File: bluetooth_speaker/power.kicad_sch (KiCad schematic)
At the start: 10 parts, among them U2 XL4015

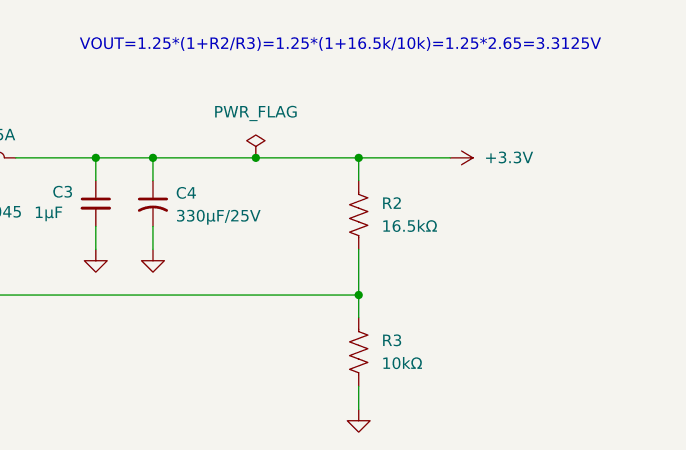
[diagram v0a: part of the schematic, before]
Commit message: adding few footprints
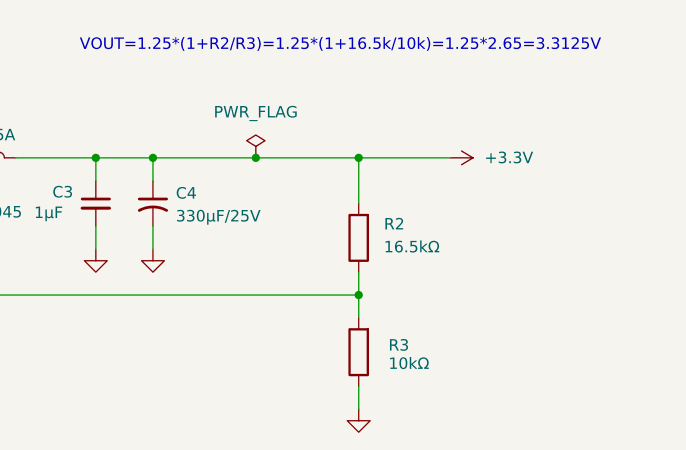
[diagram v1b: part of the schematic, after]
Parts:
- removed R2: 16.5kΩ, symbol Device:R_US
- removed R3: 10kΩ, symbol Device:R_US
- added R2: 16.5kΩ, Resistor_SMD:R_0603_1608Metric_Pad0.98x0.95mm_HandSolder, symbol Device:R
- added R3: 10kΩ, Resistor_SMD:R_0603_1608Metric_Pad0.98x0.95mm_HandSolder, symbol Device:R
- C3, C6, C7: footprint (none) -> Capacitor_SMD:C_0603_1608Metric_Pad1.08x0.95mm_HandSolder
- L1: footprint (none) -> footprints:IND_BOURNS_SDR2207
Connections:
- net +3.3V: now also R2.2
- net GND: now also R3.1
- net at U2.2 (FB): now also R2.1, R3.2
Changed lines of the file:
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@@
 	(wire
 		(pts
-			(xy 167.64 48.26) (xy 167.64 53.34)
+			(xy 167.64 50.8) (xy 167.64 53.34)
 		)
 		(stroke
@@
 	(wire
 		(pts
-			(xy 167.64 40.64) (xy 167.64 38.1)
+			(xy 167.64 43.18) (xy 167.64 38.1)
 		)
 		(stroke
@@
 	)
 	(symbol
-		(lib_id "Device:R_US")
-		(at 167.64 44.45 0)
-		(unit 1)
-		(exclude_from_sim no)
-		(in_bom yes)
-		(on_board yes)
-		(dnp no)
-		(fields_autoplaced yes)
-		(property "Reference" "R2"
-			(at 170.18 43.1799 0)
-			(effects
-				(font
-					(size 1.27 1.27)
-				)
-				(justify left)
-			)
-		)
-		(property "Value" "16.5kΩ"
-			(at 170.18 45.7199 0)
-			(effects
-				(font
-					(size 1.27 1.27)
-				)
-				(justify left)
-			)
-		)
-		(property "Footprint" ""
-			(at 168.656 44.704 90)
-			(effects
-				(font
-					(size 1.27 1.27)
-				)
-				(hide yes)
-			)
-		)
-		(property "Datasheet" "~"
-			(at 167.64 44.45 0)
-			(effects
-				(font
-					(size 1.27 1.27)
-				)
-				(hide yes)
-			)
-		)
-		(property "Description" "Resistor, US symbol"
-			(at 167.64 44.45 0)
-			(effects
-				(font
-					(size 1.27 1.27)
-				)
-				(hide yes)
-			)
-		)
-		(pin "2"
-		)
-		(pin "1"
-		)
-		(instances
-			(project "bluetooth_speaker"
-				(path "/13ff5fb5-140a-4554-92d9-4ae3849ea082/cd0ae78a-fc9d-43c8-a2e3-95882dae1290"
-					(reference "R2")
-					(unit 1)
-				)
-			)
-		)
-	)
-	(symbol
 		(lib_id "power:PWR_FLAG")
 		(at 71.12 38.1 0)
@@
 	)
 	(symbol
+		(lib_id "Device:R")
+		(at 167.64 59.69 180)
+		(unit 1)
+		(exclude_from_sim no)
+		(in_bom yes)
+		(on_board yes)
+		(dnp no)
+		(property "Reference" "R3"
+			(at 170.942 58.928 0)
+			(effects
+				(font
+					(size 1.27 1.27)
+				)
+				(justify right)
+			)
+		)
+		(property "Value" "10kΩ"
+			(at 170.942 60.96 0)
+			(effects
+				(font
+					(size 1.27 1.27)
+				)
+				(justify right)
+			)
+		)
+		(property "Footprint" "Resistor_SMD:R_0603_1608Metric_Pad0.98x0.95mm_HandSolder"
+			(at 169.418 59.69 90)
+			(effects
+				(font
+					(size 1.27 1.27)
+				)
+				(hide yes)
+			)
+		)
+		(property "Datasheet" "~"
+			(at 167.64 59.69 0)
+			(effects
+				(font
+					(size 1.27 1.27)
+				)
+				(hide yes)
+			)
+		)
+		(property "Description" "Resistor"
+			(at 167.64 59.69 0)
+			(effects
+				(font
+					(size 1.27 1.27)
+				)
+				(hide yes)
+			)
+		)
+		(pin "1"
+		)
+		(pin "2"
+		)
+		(instances
+			(project "bluetooth_speaker"
+				(path "/13ff5fb5-140a-4554-92d9-4ae3849ea082/cd0ae78a-fc9d-43c8-a2e3-95882dae1290"
+					(reference "R3")
+					(unit 1)
+				)
+			)
+		)
+	)
+	(symbol
 		(lib_id "power:GND")
 		(at 60.96 48.26 0)
@@
 			)
 		)
-		(property "Footprint" ""
+		(property "Footprint" "Capacitor_SMD:C_0603_1608Metric_Pad1.08x0.95mm_HandSolder"
 			(at 82.55 43.18 0)
 			(effects
@@
 	)
 	(symbol
-		(lib_id "Device:R_US")
-		(at 167.64 59.69 0)
-		(unit 1)
-		(exclude_from_sim no)
-		(in_bom yes)
-		(on_board yes)
-		(dnp no)
-		(fields_autoplaced yes)
-		(property "Reference" "R3"
-			(at 170.18 58.4199 0)
-			(effects
-				(font
-					(size 1.27 1.27)
-				)
-				(justify left)
-			)
-		)
-		(property "Value" "10kΩ"
-			(at 170.18 60.9599 0)
-			(effects
-				(font
-					(size 1.27 1.27)
-				)
-				(justify left)
-			)
-		)
-		(property "Footprint" ""
-			(at 168.656 59.944 90)
-			(effects
-				(font
-					(size 1.27 1.27)
-				)
-				(hide yes)
-			)
-		)
-		(property "Datasheet" "~"
-			(at 167.64 59.69 0)
-			(effects
-				(font
-					(size 1.27 1.27)
-				)
-				(hide yes)
-			)
-		)
-		(property "Description" "Resistor, US symbol"
-			(at 167.64 59.69 0)
-			(effects
-				(font
-					(size 1.27 1.27)
-				)
-				(hide yes)
-			)
-		)
-		(pin "2"
-		)
-		(pin "1"
-		)
-		(instances
-			(project "bluetooth_speaker"
-				(path "/13ff5fb5-140a-4554-92d9-4ae3849ea082/cd0ae78a-fc9d-43c8-a2e3-95882dae1290"
-					(reference "R3")
-					(unit 1)
-				)
-			)
-		)
-	)
-	(symbol
 		(lib_id "power:GND")
 		(at 119.38 48.26 0)
@@
 			)
 		)
-		(property "Footprint" ""
+		(property "Footprint" "footprints:IND_BOURNS_SDR2207"
 			(at 125.73 38.1 0)
 			(effects
@@
 	)
 	(symbol
+		(lib_id "Device:R")
+		(at 167.64 46.99 180)
+		(unit 1)
+		(exclude_from_sim no)
+		(in_bom yes)
+		(on_board yes)
+		(dnp no)
+		(property "Reference" "R2"
+			(at 170.434 45.466 0)
+			(effects
+				(font
+					(size 1.27 1.27)
+				)
+				(justify right)
+			)
+		)
+		(property "Value" "16.5kΩ"
+			(at 170.434 48.006 0)
+			(effects
+				(font
+					(size 1.27 1.27)
+				)
+				(justify right)
+			)
+		)
+		(property "Footprint" "Resistor_SMD:R_0603_1608Metric_Pad0.98x0.95mm_HandSolder"
+			(at 169.418 46.99 90)
+			(effects
+				(font
+					(size 1.27 1.27)
+				)
+				(hide yes)
+			)
+		)
+		(property "Datasheet" "~"
+			(at 167.64 46.99 0)
+			(effects
+				(font
+					(size 1.27 1.27)
+				)
+				(hide yes)
+			)
+		)
+		(property "Description" "Resistor"
+			(at 167.64 46.99 0)
+			(effects
+				(font
+					(size 1.27 1.27)
+				)
+				(hide yes)
+			)
+		)
+		(pin "1"
+		)
+		(pin "2"
+		)
+		(instances
+			(project "bluetooth_speaker"
+				(path "/13ff5fb5-140a-4554-92d9-4ae3849ea082/cd0ae78a-fc9d-43c8-a2e3-95882dae1290"
+					(reference "R2")
+					(unit 1)
+				)
+			)
+		)
+	)
+	(symbol
 		(lib_id "power:GND")
 		(at 138.43 48.26 0)
@@
 			)
 		)
-		(property "Footprint" ""
+		(property "Footprint" "Capacitor_SMD:C_0603_1608Metric_Pad1.08x0.95mm_HandSolder"
 			(at 93.98 40.64 0)
 			(effects
@@
 			)
 		)
-		(property "Footprint" ""
+		(property "Footprint" "Capacitor_SMD:C_0603_1608Metric_Pad1.08x0.95mm_HandSolder"
 			(at 138.43 43.18 0)
 			(effects

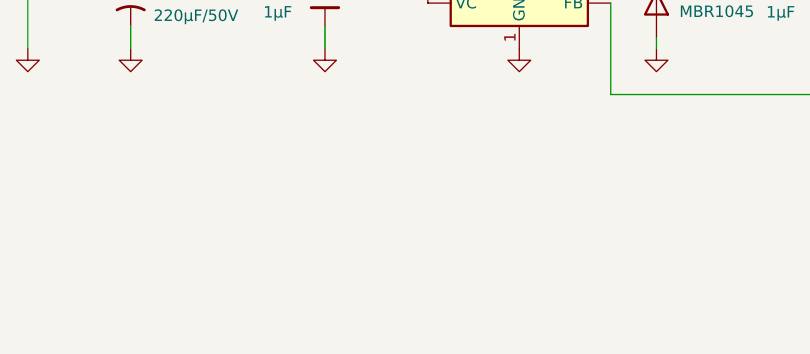
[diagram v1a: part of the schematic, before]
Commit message: Completed adding footprints, set up PCB rules
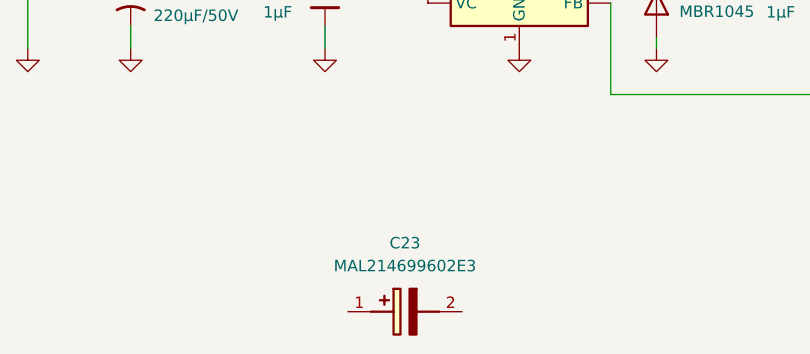
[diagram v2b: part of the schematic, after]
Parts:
- added C23: MAL214699602E3, CAPAE1050X1250N, symbol SamacSys_Parts:MAL214699602E3
- C4, C8: footprint (none) -> SamacSys_Parts:CAPAE1050X1250N
- D2: footprint Package_TO_SOT_THT:TO-220-2_Horizontal_TabDown -> Package_TO_SOT_THT:TO-220-2_Vertical
- L1: footprint footprints:IND_BOURNS_SDR2207 -> SamacSys_Parts:IHLP5050FDER470M5A
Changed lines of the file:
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@@
 			)
 		)
-		(property "Footprint" ""
+		(property "Footprint" "SamacSys_Parts:CAPAE1050X1250N"
 			(at 60.96 43.18 0)
 			(effects
@@
 			)
 		)
-		(property "Datasheet" ""
+		(property "Datasheet" "https://www.vishay.com/docs/28395/150crz.pdf"
 			(at 60.96 43.18 0)
 			(effects
@@
 			)
 		)
-		(property "Footprint" ""
+		(property "Footprint" "SamacSys_Parts:CAPAE1050X1250N"
 			(at 144.78 43.18 0)
 			(effects
@@
 			)
 		)
-		(property "Datasheet" ""
+		(property "Datasheet" "https://www.vishay.com/docs/28403/146cti.pdf"
 			(at 144.78 43.18 0)
 			(effects
@@
 	)
 	(symbol
+		(lib_id "SamacSys_Parts:MAL214699602E3")
+		(at 85.09 77.47 0)
+		(unit 1)
+		(exclude_from_sim no)
+		(in_bom yes)
+		(on_board yes)
+		(dnp no)
+		(fields_autoplaced yes)
+		(property "Reference" "C23"
+			(at 91.44 69.85 0)
+			(effects
+				(font
+					(size 1.27 1.27)
+				)
+			)
+		)
+		(property "Value" "MAL214699602E3"
+			(at 91.44 72.39 0)
+			(effects
+				(font
+					(size 1.27 1.27)
+				)
+			)
+		)
+		(property "Footprint" "CAPAE1050X1250N"
+			(at 93.98 173.66 0)
+			(effects
+				(font
+					(size 1.27 1.27)
+				)
+				(justify left top)
+				(hide yes)
+			)
+		)
+		(property "Datasheet" "https://www.vishay.com/docs/28403/146cti.pdf"
+			(at 93.98 273.66 0)
+			(effects
+				(font
+					(size 1.27 1.27)
+				)
+				(justify left top)
+				(hide yes)
+			)
+		)
+		(property "Description" "Vishay Extreme 330uF 25 V Aluminium Electrolytic Capacitor 1012, 146 CTI Series 1500 h, 2000 h, 200000 h"
+			(at 85.09 77.47 0)
+			(effects
+				(font
+					(size 1.27 1.27)
+				)
+				(hide yes)
+			)
+		)
+		(property "Height" "12.5"
+			(at 93.98 473.66 0)
+			(effects
+				(font
+					(size 1.27 1.27)
+				)
+				(justify left top)
+				(hide yes)
+			)
+		)
+		(property "Mouser Part Number" "594-MAL214699602E3"
+			(at 93.98 573.66 0)
+			(effects
+				(font
+					(size 1.27 1.27)
+				)
+				(justify left top)
+				(hide yes)
+			)
+		)
+		(property "Mouser Price/Stock" "https://www.mouser.co.uk/ProductDetail/Vishay-BC-Components/MAL214699602E3?qs=Ep9Lwju7gVrLvEu3O6DVPA%3D%3D"
+			(at 93.98 673.66 0)
+			(effects
+				(font
+					(size 1.27 1.27)
+				)
+				(justify left top)
+				(hide yes)
+			)
+		)
+		(property "Manufacturer_Name" "Vishay"
+			(at 93.98 773.66 0)
+			(effects
+				(font
+					(size 1.27 1.27)
+				)
+				(justify left top)
+				(hide yes)
+			)
+		)
+		(property "Manufacturer_Part_Number" "MAL214699602E3"
+			(at 93.98 873.66 0)
+			(effects
+				(font
+					(size 1.27 1.27)
+				)
+				(justify left top)
+				(hide yes)
+			)
+		)
+		(pin "2"
+		)
+		(pin "1"
+		)
+		(instances
+			(project ""
+				(path "/13ff5fb5-140a-4554-92d9-4ae3849ea082/cd0ae78a-fc9d-43c8-a2e3-95882dae1290"
+					(reference "C23")
+					(unit 1)
+				)
+			)
+		)
+	)
+	(symbol
 		(lib_id "power:GND")
 		(at 167.64 66.04 0)
@@
 			)
 		)
-		(property "Footprint" "footprints:IND_BOURNS_SDR2207"
+		(property "Footprint" "SamacSys_Parts:IHLP5050FDER470M5A"
 			(at 125.73 38.1 0)
 			(effects
@@
 			)
 		)
-		(property "Datasheet" "~"
+		(property "Datasheet" "https://www.mouser.com/catalog/specsheets/Vishay_ihlp-5050fd-5a.pdf"
 			(at 125.73 38.1 0)
 			(effects
@@
 			)
 		)
-		(property "Footprint" "Package_TO_SOT_THT:TO-220-2_Horizontal_TabDown"
+		(property "Footprint" "Package_TO_SOT_THT:TO-220-2_Vertical"
 			(at 114.935 43.18 0)
 			(effects

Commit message: Added missing inductor
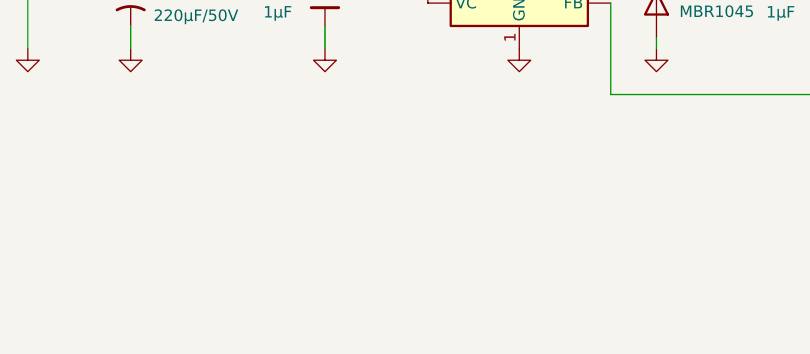
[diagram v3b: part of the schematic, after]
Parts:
- removed C23: MAL214699602E3, CAPAE1050X1250N, symbol SamacSys_Parts:MAL214699602E3
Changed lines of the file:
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@@
-	)
-	(symbol
-		(lib_id "SamacSys_Parts:MAL214699602E3")
-		(at 85.09 77.47 0)
-		(unit 1)
-		(exclude_from_sim no)
-		(in_bom yes)
-		(on_board yes)
-		(dnp no)
-		(fields_autoplaced yes)
-		(property "Reference" "C23"
-			(at 91.44 69.85 0)
-			(effects
-				(font
-					(size 1.27 1.27)
-				)
-			)
-		)
-		(property "Value" "MAL214699602E3"
-			(at 91.44 72.39 0)
-			(effects
-				(font
-					(size 1.27 1.27)
-				)
-			)
-		)
-		(property "Footprint" "CAPAE1050X1250N"
-			(at 93.98 173.66 0)
-			(effects
-				(font
-					(size 1.27 1.27)
-				)
-				(justify left top)
-				(hide yes)
-			)
-		)
-		(property "Datasheet" "https://www.vishay.com/docs/28403/146cti.pdf"
-			(at 93.98 273.66 0)
-			(effects
-				(font
-					(size 1.27 1.27)
-				)
-				(justify left top)
-				(hide yes)
-			)
-		)
-		(property "Description" "Vishay Extreme 330uF 25 V Aluminium Electrolytic Capacitor 1012, 146 CTI Series 1500 h, 2000 h, 200000 h"
-			(at 85.09 77.47 0)
-			(effects
-				(font
-					(size 1.27 1.27)
-				)
-				(hide yes)
-			)
-		)
-		(property "Height" "12.5"
-			(at 93.98 473.66 0)
-			(effects
-				(font
-					(size 1.27 1.27)
-				)
-				(justify left top)
-				(hide yes)
-			)
-		)
-		(property "Mouser Part Number" "594-MAL214699602E3"
-			(at 93.98 573.66 0)
-			(effects
-				(font
-					(size 1.27 1.27)
-				)
-				(justify left top)
-				(hide yes)
-			)
-		)
-		(property "Mouser Price/Stock" "https://www.mouser.co.uk/ProductDetail/Vishay-BC-Components/MAL214699602E3?qs=Ep9Lwju7gVrLvEu3O6DVPA%3D%3D"
-			(at 93.98 673.66 0)
-			(effects
-				(font
-					(size 1.27 1.27)
-				)
-				(justify left top)
-				(hide yes)
-			)
-		)
-		(property "Manufacturer_Name" "Vishay"
-			(at 93.98 773.66 0)
-			(effects
-				(font
-					(size 1.27 1.27)
-				)
-				(justify left top)
-				(hide yes)
-			)
-		)
-		(property "Manufacturer_Part_Number" "MAL214699602E3"
-			(at 93.98 873.66 0)
-			(effects
-				(font
-					(size 1.27 1.27)
-				)
-				(justify left top)
-				(hide yes)
-			)
-		)
-		(pin "2"
-		)
-		(pin "1"
-		)
-		(instances
-			(project ""
-				(path "/13ff5fb5-140a-4554-92d9-4ae3849ea082/cd0ae78a-fc9d-43c8-a2e3-95882dae1290"
-					(reference "C23")
-					(unit 1)
-				)
-			)
-		)
 	)
 	(symbol

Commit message: Completed the PCB design
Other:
- company: (none) -> Politechnika Poznańska
- title: (none) -> bluetooth speaker
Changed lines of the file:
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@@
 	(generator_version "9.0")
 	(paper "A4")
+	(title_block
+		(title "bluetooth speaker")
+		(date "2026-01-05")
+		(rev "1.0")
+		(company "Politechnika Poznańska")
+	)
 	(text "VOUT=1.25*(1+R2/R3)=1.25*(1+16.5k/10k)=1.25*2.65=3.3125V"
 		(exclude_from_sim no)

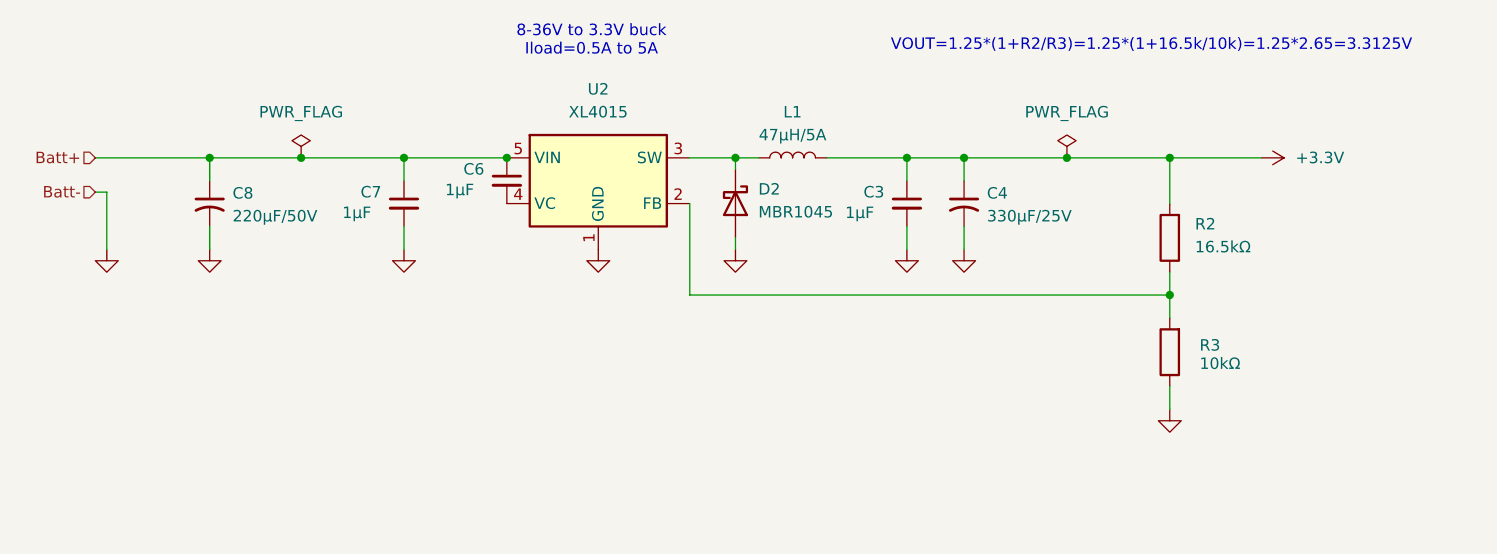
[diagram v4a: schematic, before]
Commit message: Exchanged CP2102N to CP2102C due to discontinuation
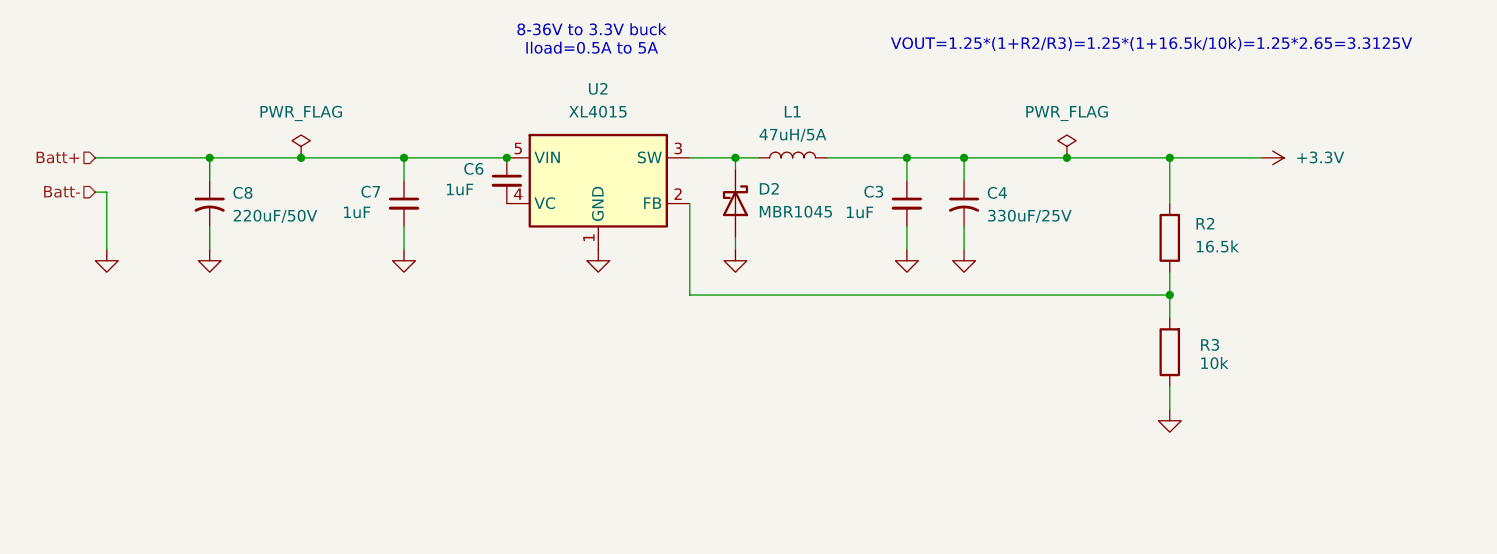
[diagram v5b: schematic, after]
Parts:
- C3, C6, C7: value 1µF -> 1uF
- C4: value 330µF/25V -> 330uF/25V
- C8: value 220µF/50V -> 220uF/50V
- L1: value 47µH/5A -> 47uH/5A
- R2: value 16.5kΩ -> 16.5k
- R3: value 10kΩ -> 10k
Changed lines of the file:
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@@
 			)
 		)
-		(property "Value" "220µF/50V"
+		(property "Value" "220uF/50V"
 			(at 63.5 44.5769 0)
 			(effects
@@
 			)
 		)
-		(property "Value" "330µF/25V"
+		(property "Value" "330uF/25V"
 			(at 147.32 44.5769 0)
 			(effects
@@
 			)
 		)
-		(property "Value" "10kΩ"
+		(property "Value" "10k"
 			(at 170.942 60.96 0)
 			(effects
@@
 			)
 		)
-		(property "Value" "1µF"
+		(property "Value" "1uF"
 			(at 75.692 44.196 0)
 			(effects
@@
 			)
 		)
-		(property "Value" "47µH/5A"
+		(property "Value" "47uH/5A"
 			(at 125.73 35.56 90)
 			(effects
@@
 			)
 		)
-		(property "Value" "16.5kΩ"
+		(property "Value" "16.5k"
 			(at 170.434 48.006 0)
 			(effects
@@
 			)
 		)
-		(property "Value" "1µF"
+		(property "Value" "1uF"
 			(at 87.122 41.656 0)
 			(effects
@@
 			)
 		)
-		(property "Value" "1µF"
+		(property "Value" "1uF"
 			(at 131.572 44.196 0)
 			(effects
